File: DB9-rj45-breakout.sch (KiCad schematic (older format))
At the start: 2 parts, among them CN1 1x9, CN2 1x8

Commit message: b toggle conf
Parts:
- added SW?: spdt, symbol switches:spdt
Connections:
- net b: now also SW?.2 (c); no longer CN2.7
- net up: now also SW?.3 (nc)
- new net: CN2.7, SW?.1 (no)
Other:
- moved on the sheet: CN1, CN2
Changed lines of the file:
@@
 L pin_headers:1x9 CN1
 U 1 1 5FBFEB21
-P 5000 3700
-F 0 "CN1" H 5400 3700 50  0000 C CNN
-F 1 "1x9" H 5000 4100 50  0001 C CNN
-F 2 "connectors:DB9" H 5000 4000 50  0001 C CNN
-F 3 "" H 5000 3800 50  0001 C CNN
-	1    5000 3700
-	-1   0    0    -1
+P 6000 3300
+F 0 "CN1" H 6400 3300 50  0000 C CNN
+F 1 "1x9" H 6000 3700 50  0001 C CNN
+F 2 "connectors:DB9" H 6000 3600 50  0001 C CNN
+F 3 "" H 6000 3400 50  0001 C CNN
+	1    6000 3300
+	1    0    0    1
 $EndComp
 Wire Wire Line
-	5000 4100 5400 4100
+	6000 2900 5600 2900
 Wire Wire Line
-	6200 3300 6700 3300
-Text Label 5100 4100 0    50   ~ 0
+	4800 3700 4300 3700
+Text Label 5900 2900 2    50   ~ 0
 GND
-Text Label 5100 4000 0    50   ~ 0
+Text Label 5900 3000 2    50   ~ 0
 5V
-Text Label 5100 3400 0    50   ~ 0
+Text Label 5900 3600 2    50   ~ 0
 up
-Text Label 5100 3500 0    50   ~ 0
+Text Label 5900 3500 2    50   ~ 0
 down
-Text Label 5100 3600 0    50   ~ 0
+Text Label 5900 3400 2    50   ~ 0
 left
-Text Label 5100 3700 0    50   ~ 0
+Text Label 5900 3300 2    50   ~ 0
 right
-Text Label 5100 3900 0    50   ~ 0
+Text Label 5900 3100 2    50   ~ 0
 a
-Text Label 5100 4200 0    50   ~ 0
+Text Label 5900 2800 2    50   ~ 0
 b
-NoConn ~ 5000 3800
+NoConn ~ 6000 3200
 Wire Wire Line
-	5000 3400 6700 3400
+	6000 3500 4300 3500
 Wire Wire Line
-	5000 3500 6700 3500
+	4300 3400 6000 3400
 Wire Wire Line
-	6700 3600 5000 3600
+	6000 3300 4300 3300
 Wire Wire Line
-	5000 3700 6700 3700
+	5600 2900 4800 3700
 Wire Wire Line
-	5400 4100 6200 3300
-Wire Wire Line
-	5000 4000 6700 4000
-Wire Wire Line
-	6000 3800 6700 3800
-Wire Wire Line
-	5900 4200 6200 3900
-Wire Wire Line
-	6200 3900 6700 3900
-Wire Wire Line
-	5000 4200 5900 4200
-Wire Wire Line
-	5900 3900 6000 3800
-Wire Wire Line
-	5000 3900 5900 3900
-Text Notes 4900 3300 2    50   ~ 0
+	6000 3000 4300 3000
+Text Notes 6100 3700 0    50   ~ 0
 amiga
-Text Notes 6800 3200 0    50   ~ 0
+Text Notes 4200 3800 2    50   ~ 0
 RJ45
 $Comp
 L pin_headers:1x8 CN2
 U 1 1 5FBFEFE7
-P 6700 3600
-F 0 "CN2" H 6792 3077 50  0000 C CNN
-F 1 "1x8" H 6700 4000 50  0001 C CNN
-F 2 "modular-jack:RJHSE-5080" H 6700 3900 50  0001 C CNN
-F 3 "" H 6700 3700 50  0001 C CNN
-	1    6700 3600
-	1    0    0    -1
+P 4300 3400
+F 0 "CN2" H 4392 2877 50  0000 C CNN
+F 1 "1x8" H 4300 3800 50  0001 C CNN
+F 2 "modular-jack:RJHSE-5080" H 4300 3700 50  0001 C CNN
+F 3 "" H 4300 3500 50  0001 C CNN
+	1    4300 3400
+	-1   0    0    1
 $EndComp
+Wire Wire Line
+	5200 3200 4300 3200
+Wire Wire Line
+	6000 3100 5300 3100
+Wire Wire Line
+	5300 3100 5200 3200
+$Comp
+L switches:spdt SW?
+U 1 1 5FD40BAE
+P 5400 2800
+F 0 "SW?" H 5400 2711 50  0000 C CNN
+F 1 "spdt" H 5400 2900 50  0001 C CNN
+F 2 "" H 5400 2800 50  0001 C CNN
+F 3 "" H 5400 2800 50  0001 C CNN
+	1    5400 2800
+	-1   0    0    1
+$EndComp
+Wire Wire Line
+	6000 2800 5500 2800
+Wire Wire Line
+	6000 3600 4600 3600
+Wire Wire Line
+	5300 2900 4600 3600
+Connection ~ 4600 3600
+Wire Wire Line
+	4600 3600 4300 3600
+Wire Wire Line
+	5300 2800 5000 3100
+Wire Wire Line
+	4300 3100 5000 3100
 $EndSCHEMATC

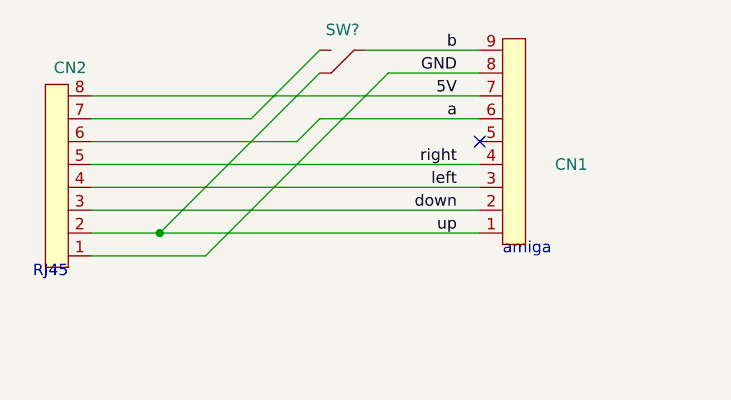
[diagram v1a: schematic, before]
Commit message: added toggle switch to select up button
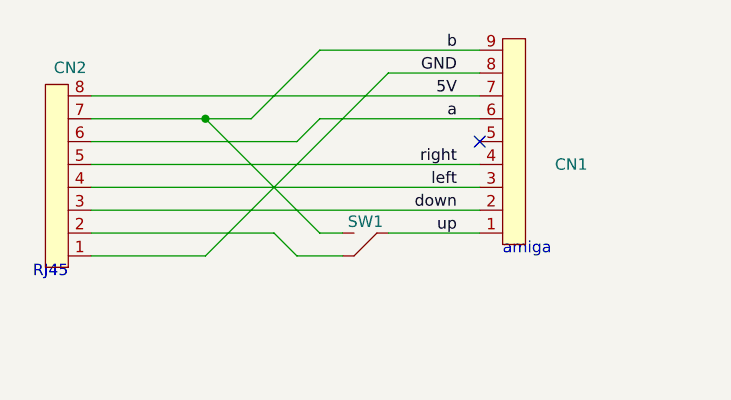
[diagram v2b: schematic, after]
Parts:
- SW1: renamed from SW?; footprint (none) -> switch:100SP1T1B4M2QE
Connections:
- net b: now also CN2.7, SW1.1 (no); no longer SW1.2 (c)
- net up: now also SW1.2 (c); no longer CN2.2, SW1.3 (nc)
- new net: CN2.2, SW1.3 (nc)
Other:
- moved on the sheet: SW1
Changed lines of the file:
@@
 	5300 3100 5200 3200
 $Comp
-L switches:spdt SW?
+L switches:spdt SW1
 U 1 1 5FD40BAE
-P 5400 2800
-F 0 "SW?" H 5400 2711 50  0000 C CNN
-F 1 "spdt" H 5400 2900 50  0001 C CNN
-F 2 "" H 5400 2800 50  0001 C CNN
-F 3 "" H 5400 2800 50  0001 C CNN
-	1    5400 2800
+P 5500 3600
+F 0 "SW1" H 5500 3550 50  0000 C CNN
+F 1 "spdt" H 5500 3700 50  0001 C CNN
+F 2 "switch:100SP1T1B4M2QE" H 5500 3600 50  0001 C CNN
+F 3 "" H 5500 3600 50  0001 C CNN
+	1    5500 3600
 	-1   0    0    1
 $EndComp
 Wire Wire Line
-	6000 2800 5500 2800
-Wire Wire Line
-	6000 3600 4600 3600
-Wire Wire Line
-	5300 2900 4600 3600
-Connection ~ 4600 3600
-Wire Wire Line
-	4600 3600 4300 3600
-Wire Wire Line
 	5300 2800 5000 3100
 Wire Wire Line
-	4300 3100 5000 3100
+	4300 3100 4800 3100
+Wire Wire Line
+	6000 3600 5600 3600
+Wire Wire Line
+	5300 3600 4800 3100
+Connection ~ 4800 3100
+Wire Wire Line
+	4800 3100 5000 3100
+Wire Wire Line
+	5300 3600 5400 3600
+Wire Wire Line
+	5400 3700 5200 3700
+Wire Wire Line
+	5200 3700 5100 3600
+Wire Wire Line
+	4300 3600 5100 3600
+Wire Wire Line
+	5300 2800 6000 2800
 $EndSCHEMATC

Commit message: fixed switch to choose 2nd button between up and 2nd button
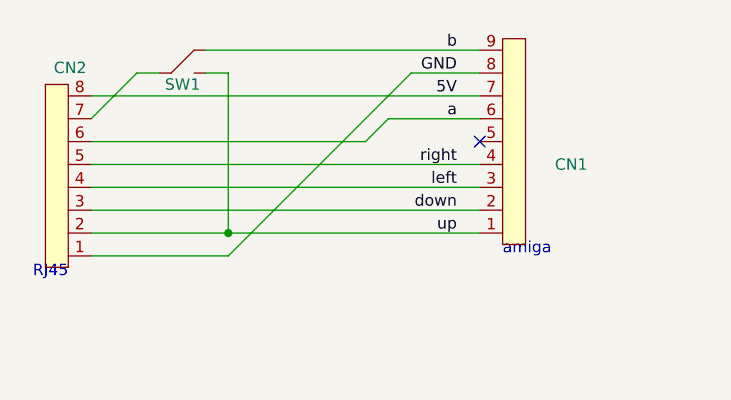
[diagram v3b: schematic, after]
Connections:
- net b: now also SW1.3 (nc); no longer CN2.7, SW1.1 (no)
- net up: now also CN2.2, SW1.1 (no); no longer SW1.2 (c)
- new net: CN2.7, SW1.2 (c)
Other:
- moved on the sheet: SW1
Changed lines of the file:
@@
 $EndComp
 Wire Wire Line
-	6000 2900 5600 2900
+	6000 2900 5700 2900
 Wire Wire Line
-	4800 3700 4300 3700
+	4900 3700 4300 3700
 Text Label 5900 2900 2    50   ~ 0
 GND
@@
 	6000 3300 4300 3300
 Wire Wire Line
-	5600 2900 4800 3700
+	5700 2900 4900 3700
 Wire Wire Line
 	6000 3000 4300 3000
@@
 $EndComp
 Wire Wire Line
-	5200 3200 4300 3200
+	5500 3200 4300 3200
 Wire Wire Line
-	6000 3100 5300 3100
+	6000 3100 5600 3100
 Wire Wire Line
-	5300 3100 5200 3200
+	5600 3100 5500 3200
 $Comp
 L switches:spdt SW1
 U 1 1 5FD40BAE
-P 5500 3600
-F 0 "SW1" H 5500 3550 50  0000 C CNN
-F 1 "spdt" H 5500 3700 50  0001 C CNN
-F 2 "switch:100SP1T1B4M2QE" H 5500 3600 50  0001 C CNN
-F 3 "" H 5500 3600 50  0001 C CNN
-	1    5500 3600
-	-1   0    0    1
+P 4700 2900
+F 0 "SW1" H 4700 2850 50  0000 C CNN
+F 1 "spdt" H 4700 3000 50  0001 C CNN
+F 2 "switch:100SP1T1B4M2QE" H 4700 2900 50  0001 C CNN
+F 3 "" H 4700 2900 50  0001 C CNN
+	1    4700 2900
+	1    0    0    -1
 $EndComp
 Wire Wire Line
-	5300 2800 5000 3100
+	4300 3100 4500 2900
 Wire Wire Line
-	4300 3100 4800 3100
+	4500 2900 4600 2900
 Wire Wire Line
-	6000 3600 5600 3600
+	4800 2800 6000 2800
 Wire Wire Line
-	5300 3600 4800 3100
-Connection ~ 4800 3100
+	4300 3600 4900 3600
 Wire Wire Line
-	4800 3100 5000 3100
+	4900 2900 4900 3600
 Wire Wire Line
-	5300 3600 5400 3600
+	4900 2900 4800 2900
+Connection ~ 4900 3600
 Wire Wire Line
-	5400 3700 5200 3700
-Wire Wire Line
-	5200 3700 5100 3600
-Wire Wire Line
-	4300 3600 5100 3600
-Wire Wire Line
-	5300 2800 6000 2800
+	4900 3600 6000 3600
 $EndSCHEMATC

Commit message: slimmed board down so the DB9 connector can be cut to size
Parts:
- CN1: footprint connectors:DB9 -> connectors:DB9-slim
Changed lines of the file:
@@
 F 0 "CN1" H 6400 3300 50  0000 C CNN
 F 1 "1x9" H 6000 3700 50  0001 C CNN
-F 2 "connectors:DB9" H 6000 3600 50  0001 C CNN
+F 2 "connectors:DB9-slim" H 6000 3600 50  0001 C CNN
 F 3 "" H 6000 3400 50  0001 C CNN
 	1    6000 3300

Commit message: changed DB9 pinout to female
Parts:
- CN1: footprint connectors:DB9-slim -> connectors:DB9-slim-female
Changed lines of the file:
@@
 F 0 "CN1" H 6400 3300 50  0000 C CNN
 F 1 "1x9" H 6000 3700 50  0001 C CNN
-F 2 "connectors:DB9-slim" H 6000 3600 50  0001 C CNN
+F 2 "connectors:DB9-slim-female" H 6000 3600 50  0001 C CNN
 F 3 "" H 6000 3400 50  0001 C CNN
 	1    6000 3300
